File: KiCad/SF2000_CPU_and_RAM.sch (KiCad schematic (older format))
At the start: 6 parts, among them U10 IS61WV20488FBLL-10TLI, U11 IS61WV20488FBLL-10TLI, U12 IS61WV20488FBLL-10TLI, U13 IS61WV20488FBLL-10TLI, U9 68000D

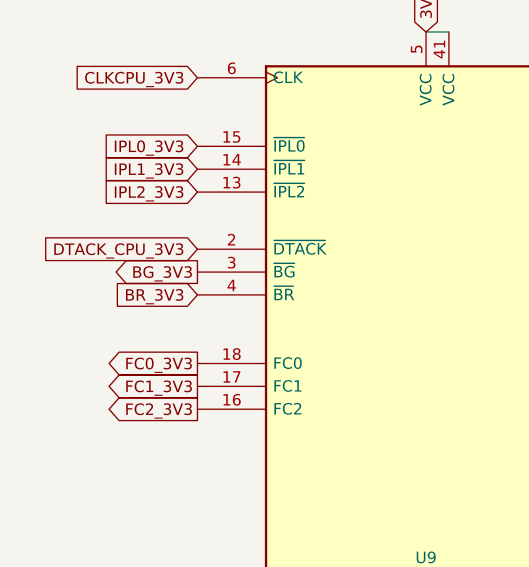
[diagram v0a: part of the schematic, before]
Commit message: Separated BR_3V3, BG_3V3 --> BR_CPU_3V3, BG_CPU_3V3, BR_3V3, BG_3V3 (removed XRDY, INT6 and used those pins for BR_3V3, BG_3V3)
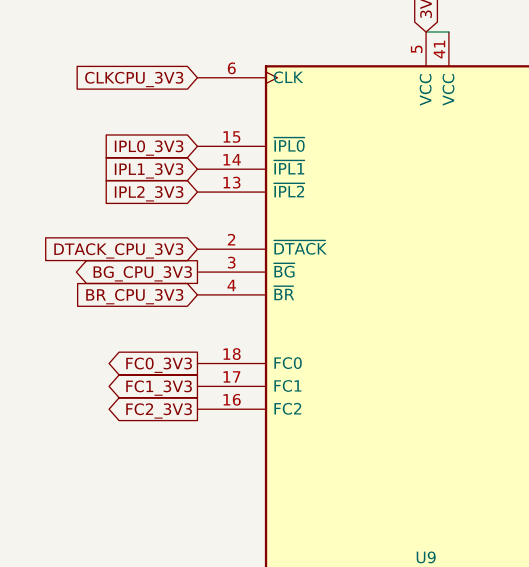
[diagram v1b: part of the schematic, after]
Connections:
- net labels added: BG_CPU_3V3, BR_CPU_3V3
- net labels removed: BG_3V3, BR_3V3
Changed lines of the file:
@@
 A23_3V3
 Text GLabel 1500 2350 0    50   Output ~ 0
-BG_3V3
+BG_CPU_3V3
 Text GLabel 3500 3950 2    50   BiDi ~ 0
 D0_3V3
@@
 HLT_3V3
 Text GLabel 1500 2450 0    50   Input ~ 0
-BR_3V3
+BR_CPU_3V3
 Text GLabel 1500 2250 0    50   Input ~ 0
 DTACK_CPU_3V3

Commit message: changed to custom QFP-64 footprint for the 68SEC000
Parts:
- U9: footprint Package_QFP:LQFP-64_14x14mm_P0.8mm -> SF2000:QFP-64_14x14mm_Pitch0.8mm
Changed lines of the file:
@@
 F 0 "U9" H 2500 3800 50  0000 C CNN
 F 1 "68000D" H 2500 3700 50  0000 C CNN
-F 2 "Package_QFP:LQFP-64_14x14mm_P0.8mm" H 2500 3700 50  0001 C CNN
+F 2 "SF2000:QFP-64_14x14mm_Pitch0.8mm" H 2500 3700 50  0001 C CNN
 F 3 "https://www.nxp.com/docs/en/reference-manual/MC68000UM.pdf" H 2500 3700 50  0001 C CNN
 	1    2500 3700

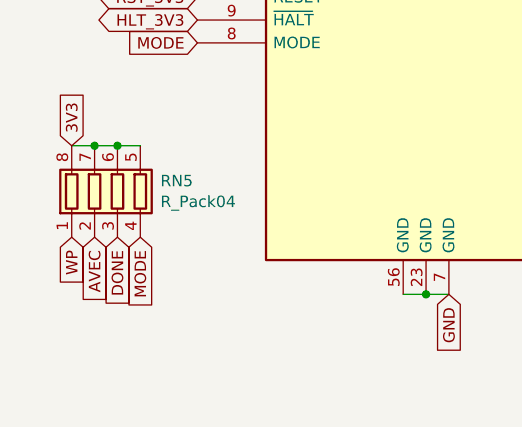
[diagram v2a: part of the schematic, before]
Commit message: Renamed DONE to CDONE and routed track
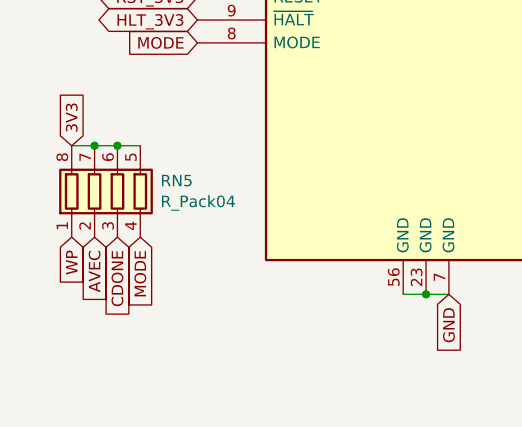
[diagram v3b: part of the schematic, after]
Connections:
- net labels added: CDONE
- net labels removed: DONE
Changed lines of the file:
@@
 AVEC
 Text GLabel 1150 5850 3    50   Input ~ 0
-DONE
+CDONE
 Text GLabel 950  5850 3    50   Input ~ 0
 WP

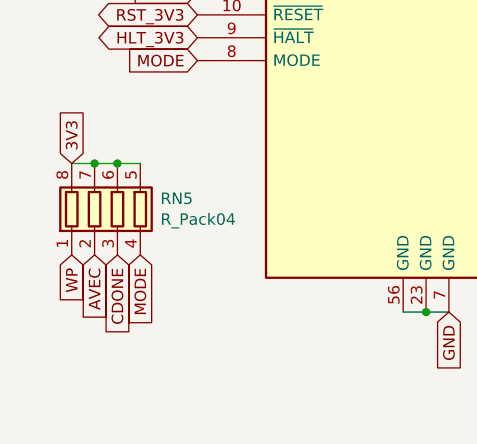
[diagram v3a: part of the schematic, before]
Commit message: Removed WP# and FLASH_BUSY signals
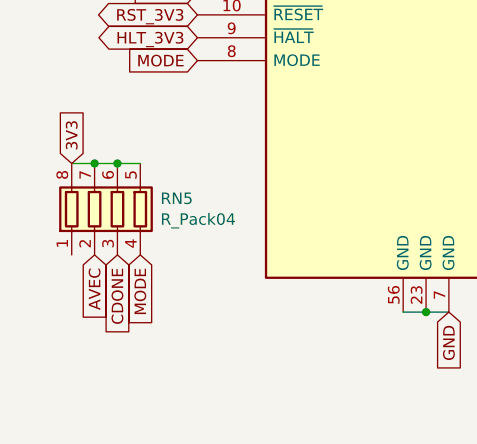
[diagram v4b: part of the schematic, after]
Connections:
- net labels removed: WP
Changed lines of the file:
@@
 Text GLabel 1150 5850 3    50   Input ~ 0
 CDONE
-Text GLabel 950  5850 3    50   Input ~ 0
-WP
 $EndSCHEMATC

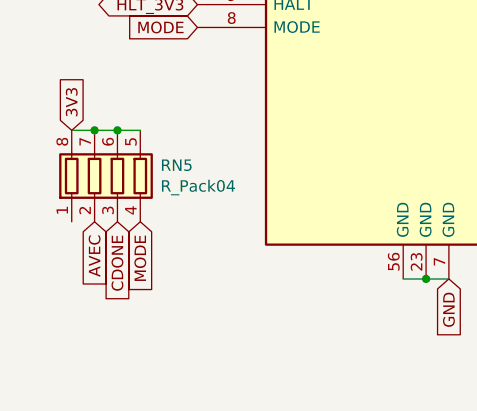
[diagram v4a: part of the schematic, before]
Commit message: Assign FLASH_WE signal to FPGA pin 74 (GPIOR_158_TEST_N) and to 10k resistor array pin 1 in RN5
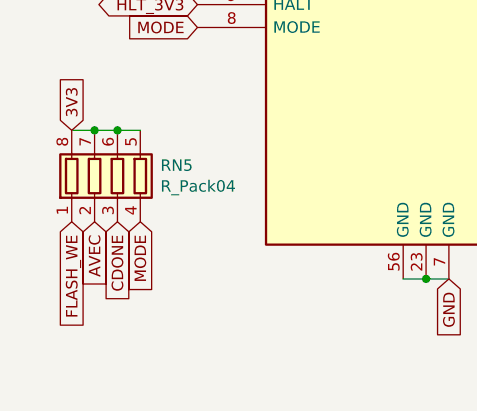
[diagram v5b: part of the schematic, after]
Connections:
- net labels added: FLASH_WE
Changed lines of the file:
@@
 Text GLabel 1150 5850 3    50   Input ~ 0
 CDONE
+Text GLabel 950  5850 3    50   Input ~ 0
+FLASH_WE
 $EndSCHEMATC

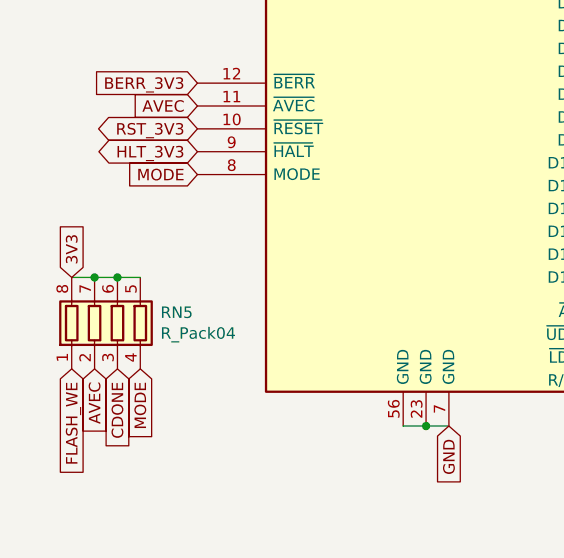
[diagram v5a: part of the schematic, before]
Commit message: Remove MODE from pull-up resistor RN5 as it can be left floating for 16-bit mode according to MC68000UM
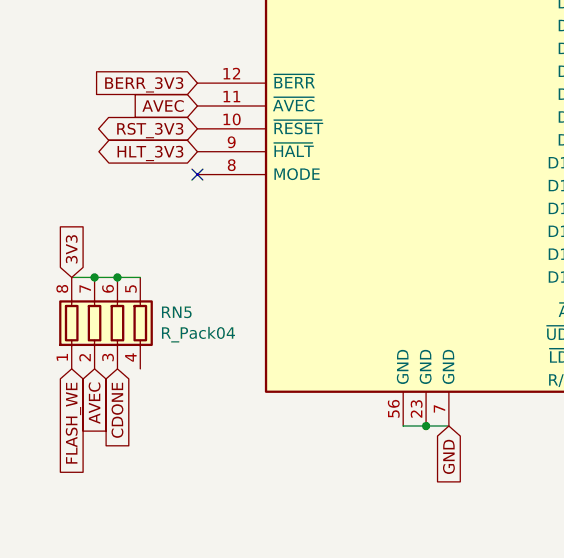
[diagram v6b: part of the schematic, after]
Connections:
- net labels removed: MODE
- no-connect marks 1 -> 2
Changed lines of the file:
@@
 Wire Wire Line
 	1150 5450 1250 5450
-Text GLabel 1500 5000 0    50   Input ~ 0
-MODE
-Text GLabel 1250 5850 3    50   Input ~ 0
-MODE
 Text GLabel 1500 4700 0    50   Input ~ 0
 AVEC
@@
 Text GLabel 950  5850 3    50   Input ~ 0
 FLASH_WE
+NoConn ~ 1500 5000
 $EndSCHEMATC

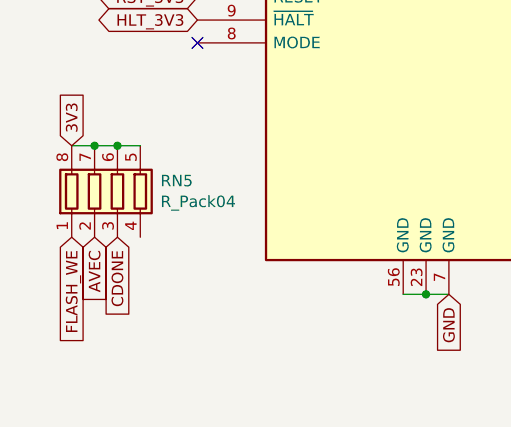
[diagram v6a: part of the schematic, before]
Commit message: swap position between AVEC and CDONE in resistor array RN5 and fix routing of those signals
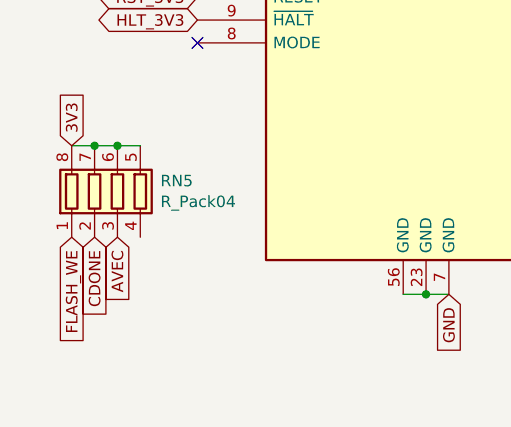
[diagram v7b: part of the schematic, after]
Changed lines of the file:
@@
 Text GLabel 1500 4700 0    50   Input ~ 0
 AVEC
+Text GLabel 1150 5850 3    50   Input ~ 0
+AVEC
 Text GLabel 1050 5850 3    50   Input ~ 0
-AVEC
-Text GLabel 1150 5850 3    50   Input ~ 0
 CDONE
 Text GLabel 950  5850 3    50   Input ~ 0

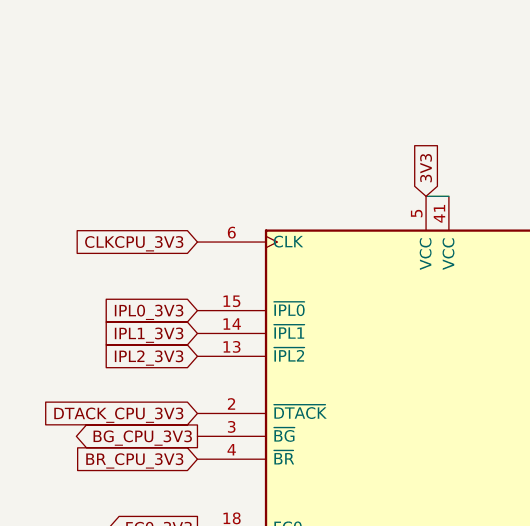
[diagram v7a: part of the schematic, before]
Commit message: Routing of clock line from FPGA to CPU (CLKCPU-line)
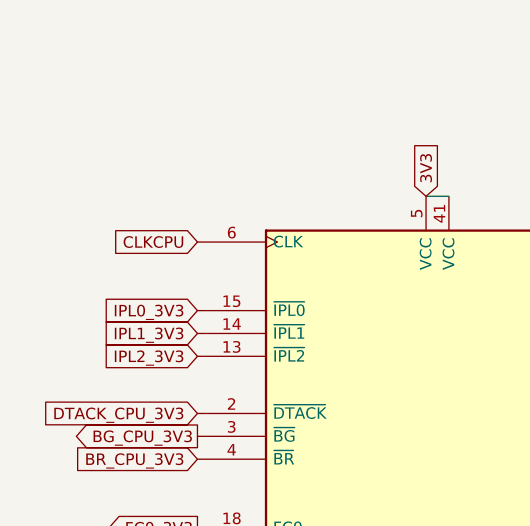
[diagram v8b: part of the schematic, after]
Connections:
- net labels added: CLKCPU
- net labels removed: CLKCPU_3V3
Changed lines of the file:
@@
 $EndComp
 Text GLabel 1500 1500 0    50   Input ~ 0
-CLKCPU_3V3
+CLKCPU
 Text GLabel 3500 2000 2    50   Output ~ 0
 A5_3V3
